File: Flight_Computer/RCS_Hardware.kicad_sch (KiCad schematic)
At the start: 68 parts, among them J1 SWD, J10 Motor, J2 TYPE-C-31-M-12, J3 I2C, J4 5V, J5 GND, J6 AMT102, J7 FC_RF, J9 AMT102, Q1 2N7002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

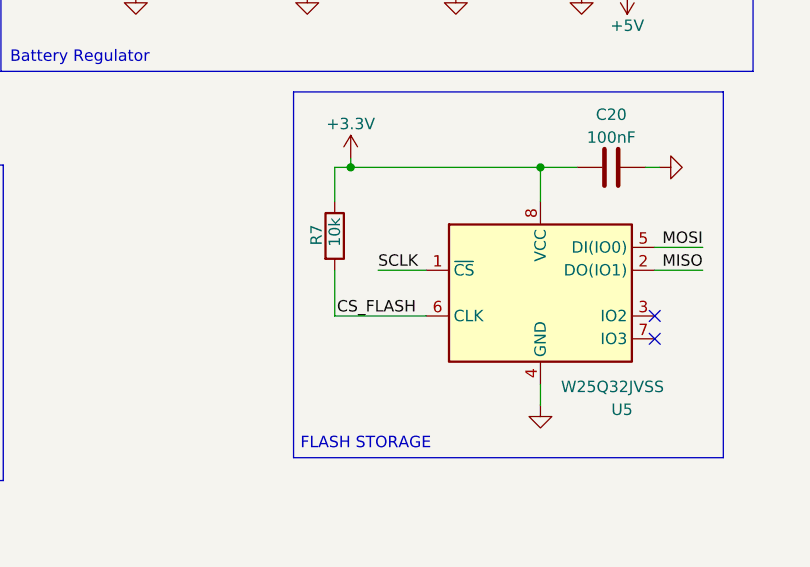
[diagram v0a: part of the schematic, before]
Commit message: Created folders for encoder, tmp, flash
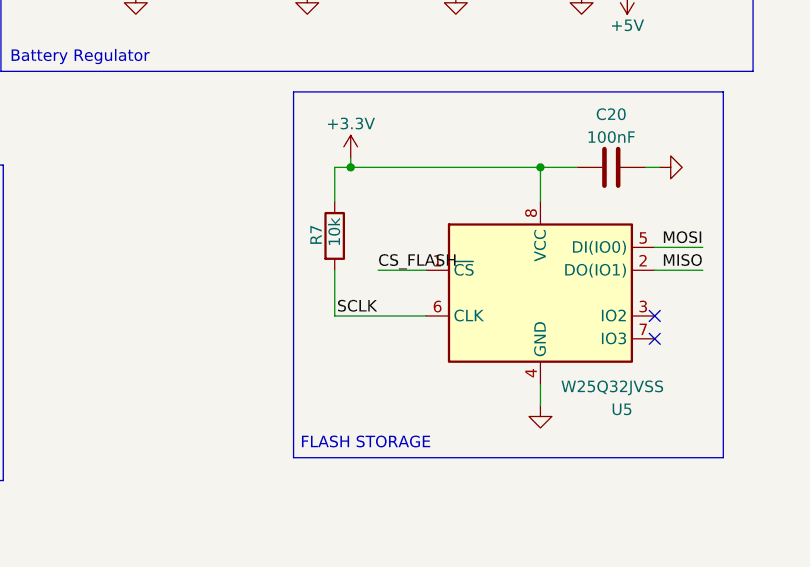
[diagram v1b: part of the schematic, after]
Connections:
- net CS_FLASH: now also U5.1 (~{CS}); no longer R7.2, U5.6 (CLK)
- net SCLK: now also R7.2, U5.6 (CLK); no longer U5.1 (~{CS})
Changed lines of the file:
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@@
 		)
 	)
-	(label "CS_FLASH"
+	(label "SCLK"
 		(at 198.882 207.518 0)
 		(fields_autoplaced yes)
@@
 		)
 	)
-	(label "SCLK"
+	(label "CS_FLASH"
 		(at 203.454 202.438 0)
 		(fields_autoplaced yes)

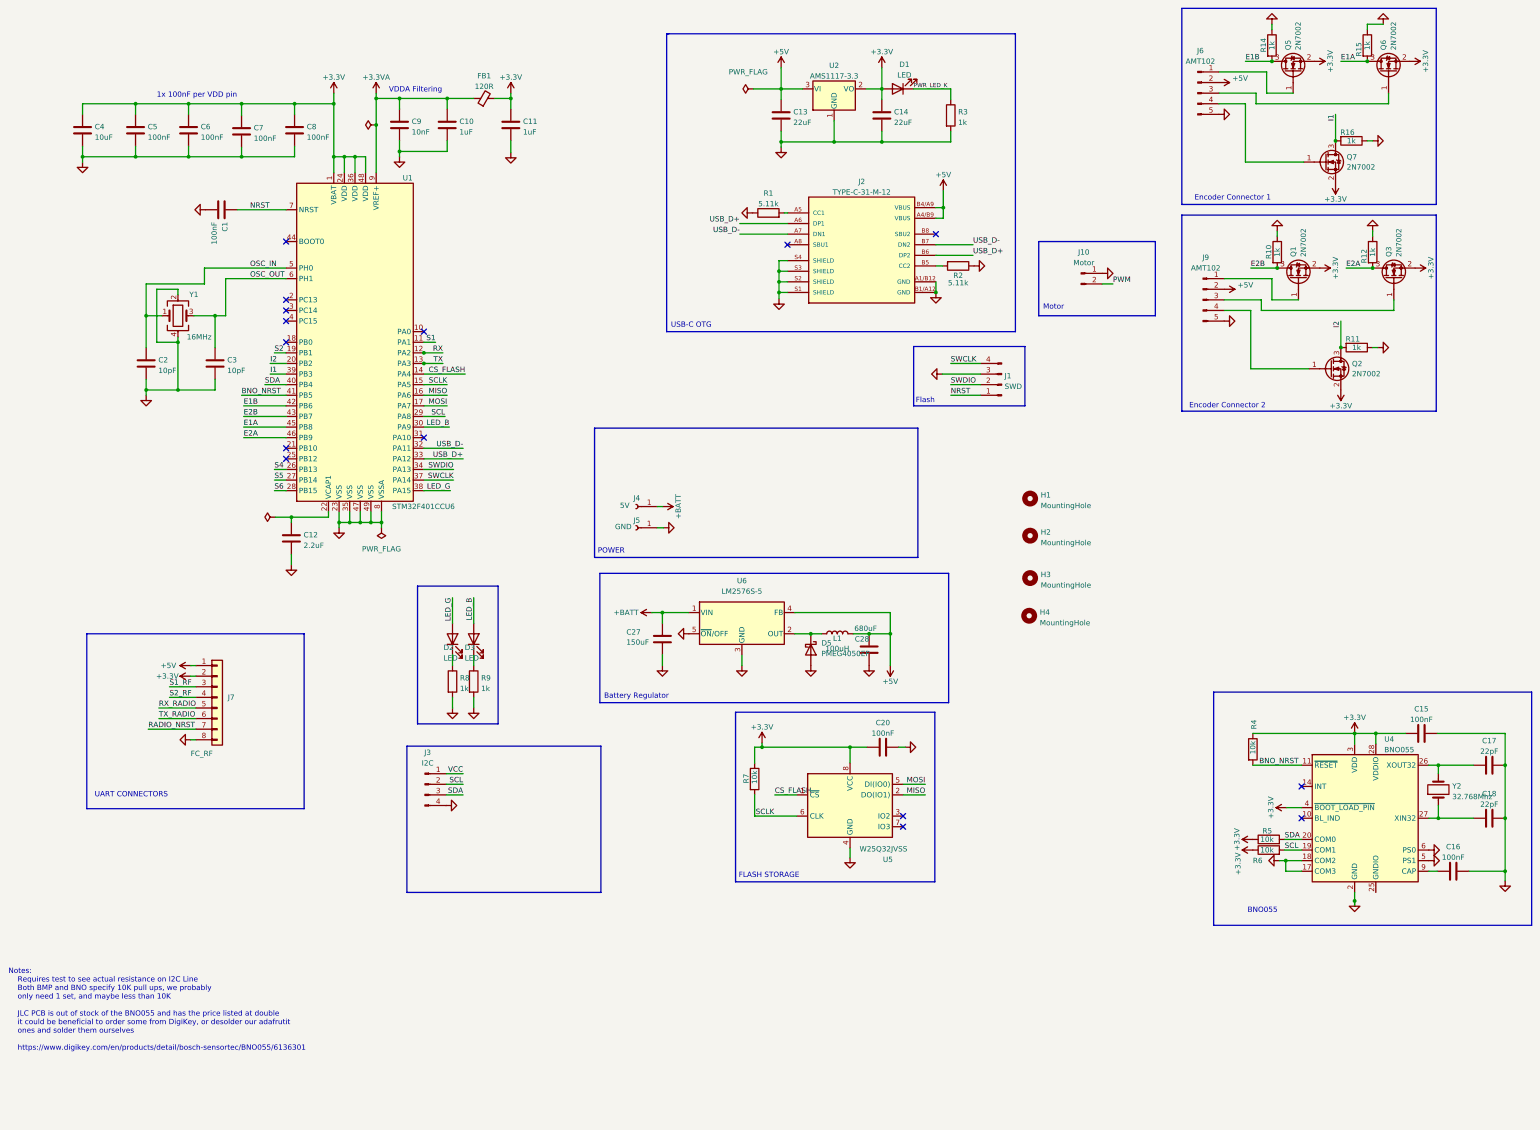
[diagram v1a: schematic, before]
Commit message: updated gyroscope schematic
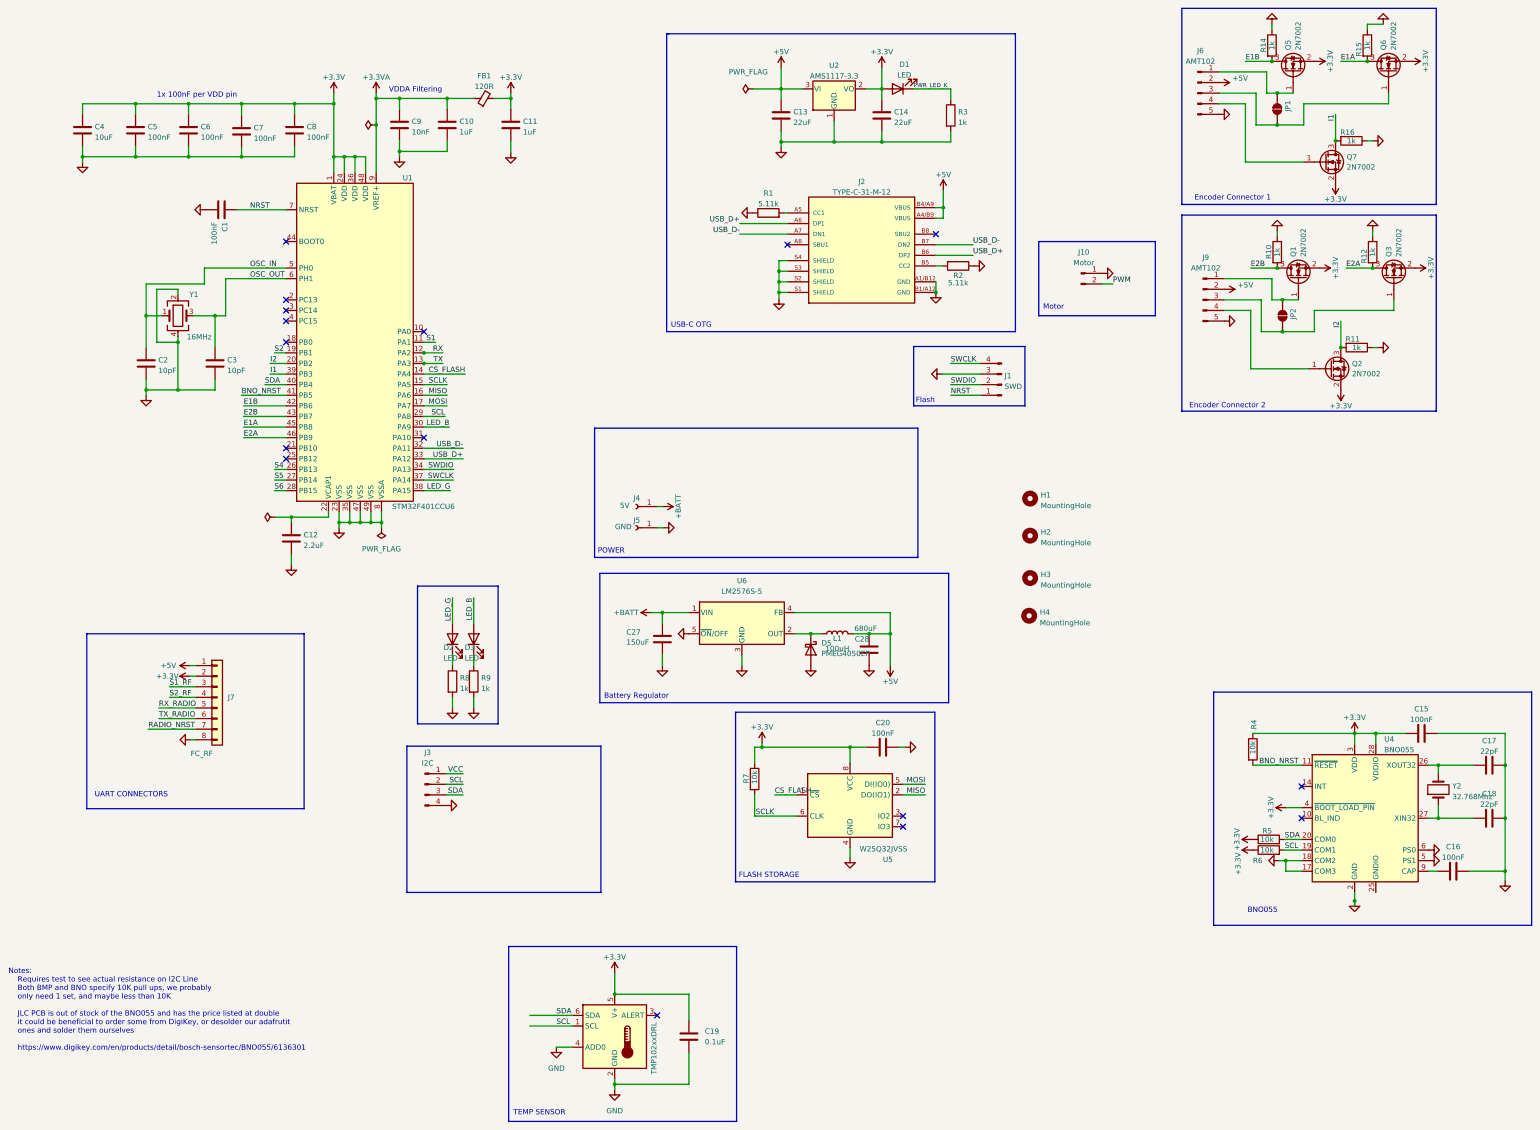
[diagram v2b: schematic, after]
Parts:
- added C19: 0.1uF, symbol Device:C
- added JP1, JP2: SolderJumper_2_Open, symbol Jumper:SolderJumper_2_Open
- added U3: TMP102xxDRL, Package_TO_SOT_SMD:SOT-563, symbol Sensor_Temperature:TMP102xxDRL
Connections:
- net +3.3V: now also C19.1, U3.5 (V+)
- net GND: now also C19.2, U3.2 (GND), U3.4 (ADD0)
- net SCL: now also U3.1 (SCL)
- net SDA: now also U3.6 (SDA)
- net at J6.3 (Pin_3), Q6.1 (G): now also JP1.1 (A)
- net at J9.1 (Pin_1), Q1.1 (G): now also JP2.2 (B)
- net at J9.3 (Pin_3), Q3.1 (G): now also JP2.1 (A)
- net at J6.1 (Pin_1), Q5.1 (G): now also JP1.2 (B)
- no-connect marks 15 -> 16
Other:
- note added: "TEMP SENSOR"

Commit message: placed components on gyroscope PCB
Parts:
- C19: footprint (none) -> Capacitor_SMD:C_0402_1005Metric
- J10: footprint (none) -> Connector_PinHeader_2.54mm:PinHeader_1x02_P2.54mm_Vertical
- J3: footprint (none) -> Connector_PinHeader_2.54mm:PinHeader_1x04_P2.54mm_Vertical
- J6, J9: footprint (none) -> Connector_PinHeader_2.54mm:PinHeader_1x05_P2.54mm_Vertical
- JP1, JP2: footprint (none) -> Jumper:SolderJumper-2_P1.3mm_Open_RoundedPad1.0x1.5mm
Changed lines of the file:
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@@
 			)
 		)
-		(property "Footprint" ""
+		(property "Footprint" "Connector_PinHeader_2.54mm:PinHeader_1x04_P2.54mm_Vertical"
 			(at 119.634 199.898 0)
 			(effects
@@
 			)
 		)
-		(property "Footprint" ""
+		(property "Footprint" "Jumper:SolderJumper-2_P1.3mm_Open_RoundedPad1.0x1.5mm"
 			(at 325.12 87.63 0)
 			(effects
@@
 			)
 		)
-		(property "Footprint" ""
+		(property "Footprint" "Connector_PinHeader_2.54mm:PinHeader_1x02_P2.54mm_Vertical"
 			(at 276.86 77.47 0)
 			(effects
@@
 			)
 		)
-		(property "Footprint" ""
+		(property "Footprint" "Capacitor_SMD:C_0402_1005Metric"
 			(at 183.8452 264.16 0)
 			(effects
@@
 			)
 		)
-		(property "Footprint" ""
+		(property "Footprint" "Jumper:SolderJumper-2_P1.3mm_Open_RoundedPad1.0x1.5mm"
 			(at 323.85 38.1 0)
 			(effects
@@
 			)
 		)
-		(property "Footprint" ""
+		(property "Footprint" "Connector_PinHeader_2.54mm:PinHeader_1x05_P2.54mm_Vertical"
 			(at 304.8 34.29 0)
 			(effects
@@
 			)
 		)
-		(property "Footprint" ""
+		(property "Footprint" "Connector_PinHeader_2.54mm:PinHeader_1x05_P2.54mm_Vertical"
 			(at 306.07 83.82 0)
 			(effects

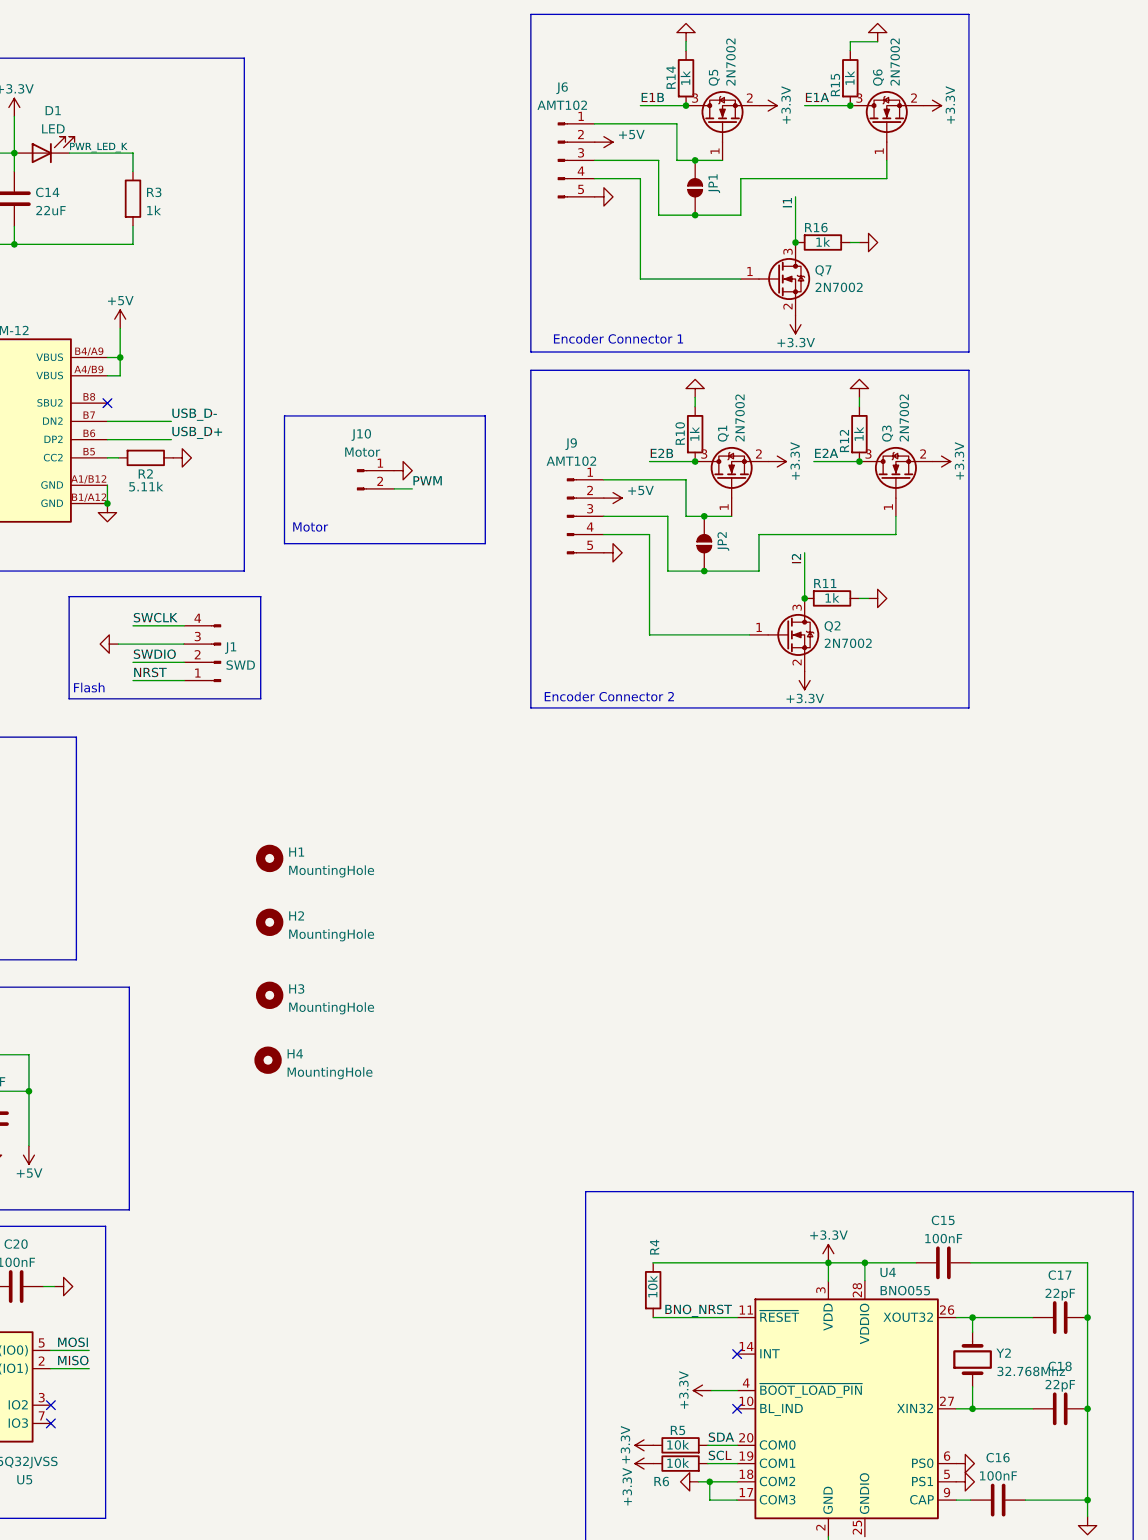
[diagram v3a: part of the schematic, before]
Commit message: routed most of pcb and updated encoder level-shifting circuit
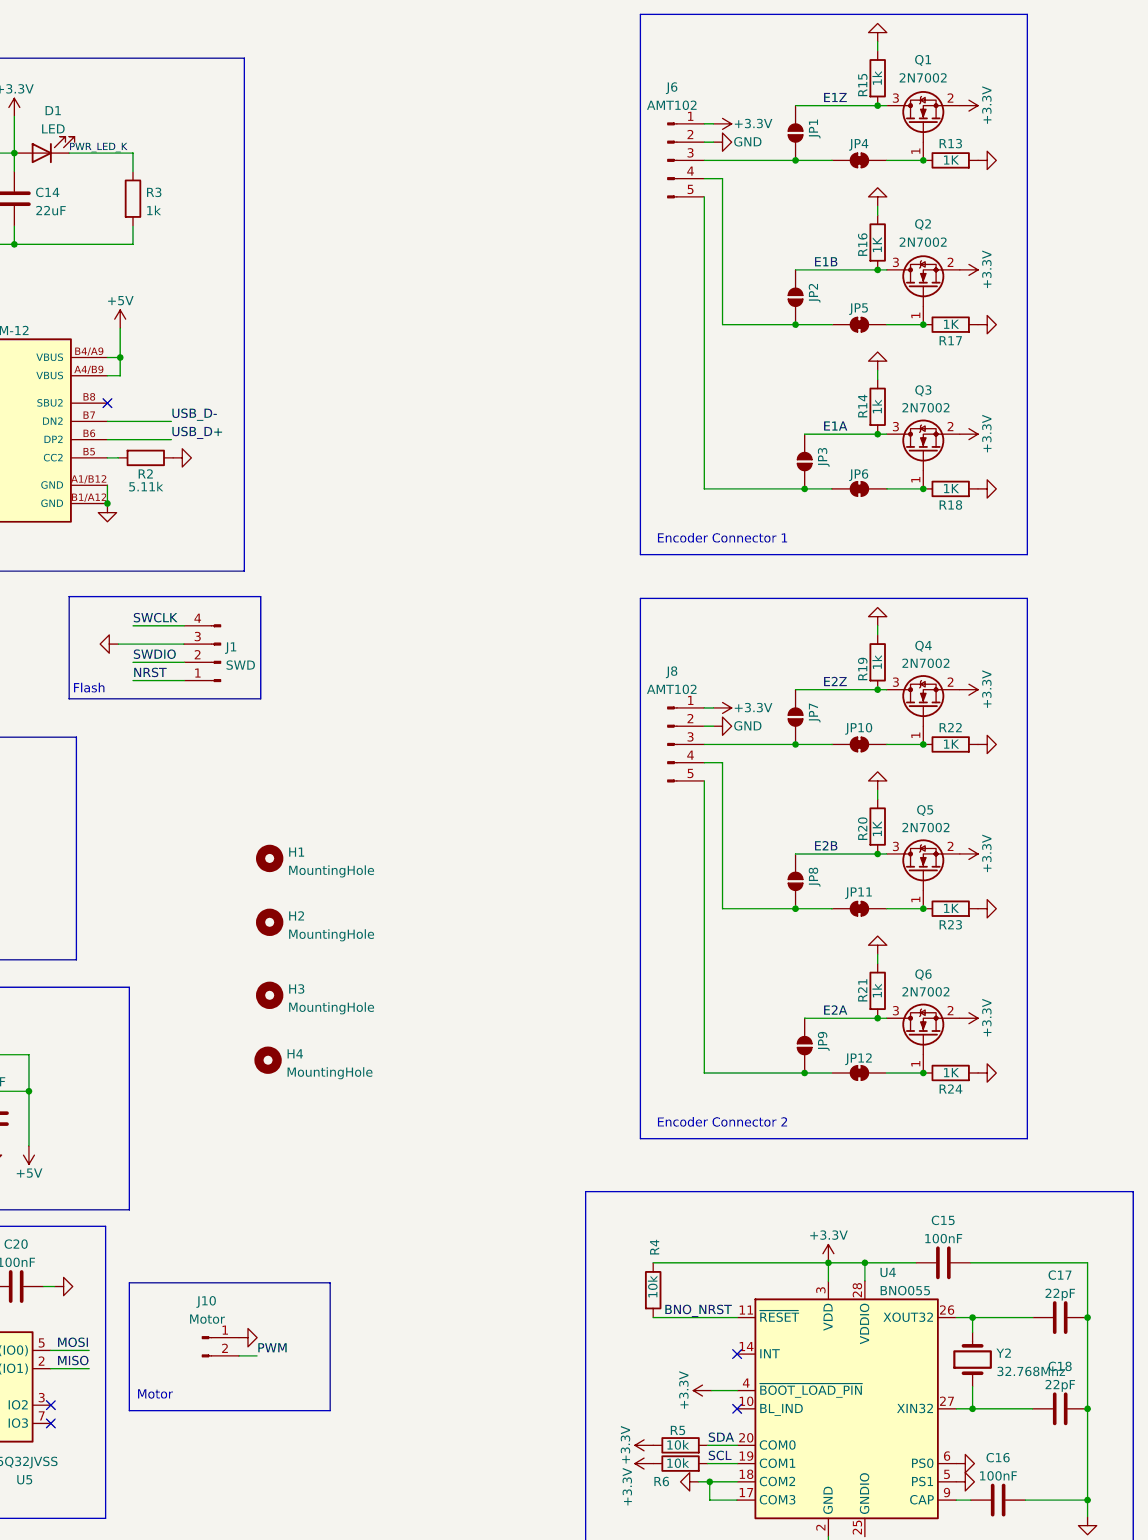
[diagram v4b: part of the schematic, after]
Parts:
- removed J9: AMT102, Connector_PinHeader_2.54mm:PinHeader_1x05_P2.54mm_Vertical, symbol Connector:Conn_01x05_Pin
- removed Q1, Q2, Q3: 2N7002, Package_TO_SOT_SMD:SOT-23, symbol Transistor_FET:2N7002
- removed R10, R11, R12: 1k, Resistor_SMD:R_0402_1005Metric, symbol Device:R
- added J8: AMT102, Connector_PinHeader_2.54mm:PinHeader_1x05_P2.54mm_Vertical, symbol Connector:Conn_01x05_Pin
- added JP10, JP11, JP12, JP4, JP5, JP6: SolderJumper_2_Bridged, Jumper:SolderJumper-2_P1.3mm_Bridged_RoundedPad1.0x1.5mm, symbol Jumper:SolderJumper_2_Bridged
- added JP3, JP7, JP8, JP9: SolderJumper_2_Open, Jumper:SolderJumper-2_P1.3mm_Open_RoundedPad1.0x1.5mm, symbol Jumper:SolderJumper_2_Open
- added Q4, Q5, Q6: 2N7002, Package_TO_SOT_SMD:SOT-23, symbol Transistor_FET:2N7002
- added R13, R17, R18, R20, R22, R23, R24: 1K, Resistor_SMD:R_0402_1005Metric, symbol Device:R
- added R19, R21: 1k, Resistor_SMD:R_0402_1005Metric, symbol Device:R
- R16: value 1k -> 1K; LCSC Part C102758 -> (none)
- renumbered Q6 to Q1, Q7 to Q2, Q5 to Q3
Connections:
- net +3.3V: now also J6.1 (Pin_1), J8.1 (Pin_1), Q4.2 (S), Q5.2 (S), Q6.2 (S)
- net +5V: no longer J6.2 (Pin_2)
- net E1A: now also Q3.3 (D), R14.2, JP3.2 (B); no longer Q1.3 (D), R15.2
- net E1B: now also JP2.2 (B), Q2.3 (D), R16.2; no longer Q3.3 (D), R14.2
- net E2A: now also JP9.2 (B), Q6.3 (D), R21.2
- net E2B: now also JP8.2 (B), Q5.3 (D), R20.2
- net GND: now also J6.2 (Pin_2), J8.2 (Pin_2), R13.2, R17.2, R18.2, R19.1, R20.1, R21.1, R22.2, R23.2, R24.2; no longer J6.5 (Pin_5)
- net I1: no longer Q2.3 (D), R16.2
- net at Q2.1 (G): now also JP5.2 (B), R17.1; no longer J6.4 (Pin_4)
- net at JP2.1 (A): now also J6.4 (Pin_4), JP5.1 (A)
- net at J6.3 (Pin_3), JP1.1 (A): now also JP4.1 (A); no longer Q1.1 (G)
- new net: JP4.2 (B), Q1.1 (G), R13.1
- new net: J8.5 (Pin_5), JP12.1 (A), JP9.1 (A)
- new net: JP12.2 (B), Q6.1 (G), R24.1
- new net: J8.4 (Pin_4), JP11.1 (A), JP8.1 (A)
- new net: J8.3 (Pin_3), JP10.1 (A), JP7.1 (A)
- new net: JP6.2 (B), Q3.1 (G), R18.1
- new net: JP10.2 (B), Q4.1 (G), R22.1
- new net: JP11.2 (B), Q5.1 (G), R23.1
- new net: J6.5 (Pin_5), JP3.1 (A), JP6.1 (A)
- new net E1Z: JP1.2 (B), Q1.3 (D), R15.2
- new net E2Z: JP7.2 (B), Q4.3 (D), R19.2
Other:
- moved on the sheet: J10, J6, Q1, Q2, Q3, R14, R15

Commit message: updated encoder and motor connectors
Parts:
- J10: footprint Connector_PinHeader_2.54mm:PinHeader_1x02_P2.54mm_Vertical -> Connector_JST:JST_SH_SM02B-SRSS-TB_1x02-1MP_P1.00mm_Horizontal
- J6, J8: footprint Connector_PinHeader_2.54mm:PinHeader_1x05_P2.54mm_Vertical -> Connector_JST:JST_SH_SM05B-SRSS-TB_1x05-1MP_P1.00mm_Horizontal
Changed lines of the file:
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@@
 			)
 		)
-		(property "Footprint" "Connector_PinHeader_2.54mm:PinHeader_1x02_P2.54mm_Vertical"
+		(property "Footprint" "Connector_JST:JST_SH_SM02B-SRSS-TB_1x02-1MP_P1.00mm_Horizontal"
 			(at 255.27 198.12 0)
 			(effects
@@
 			)
 		)
-		(property "Footprint" "Connector_PinHeader_2.54mm:PinHeader_1x05_P2.54mm_Vertical"
+		(property "Footprint" "Connector_JST:JST_SH_SM05B-SRSS-TB_1x05-1MP_P1.00mm_Horizontal"
 			(at 320.04 115.57 0)
 			(effects
@@
 		(on_board yes)
 		(dnp no)
-		(fields_autoplaced yes)
 		(property "Reference" "J6"
 			(at 320.675 24.13 0)
@@
 			)
 		)
-		(property "Footprint" "Connector_PinHeader_2.54mm:PinHeader_1x05_P2.54mm_Vertical"
+		(property "Footprint" "Connector_JST:JST_SH_SM05B-SRSS-TB_1x05-1MP_P1.00mm_Horizontal"
 			(at 320.04 34.29 0)
 			(effects
